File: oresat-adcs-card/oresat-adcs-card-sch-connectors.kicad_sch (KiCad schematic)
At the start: 14 parts, among them J1 J-SAMTEC-TFM-120-X1-XXX-D-RA, J3 Mezzanine Plug, J4 Mezzanine Plug, J5 Mezzanine Plug, J6 Mezzanine Plug, J7 Magnetorquer Pins

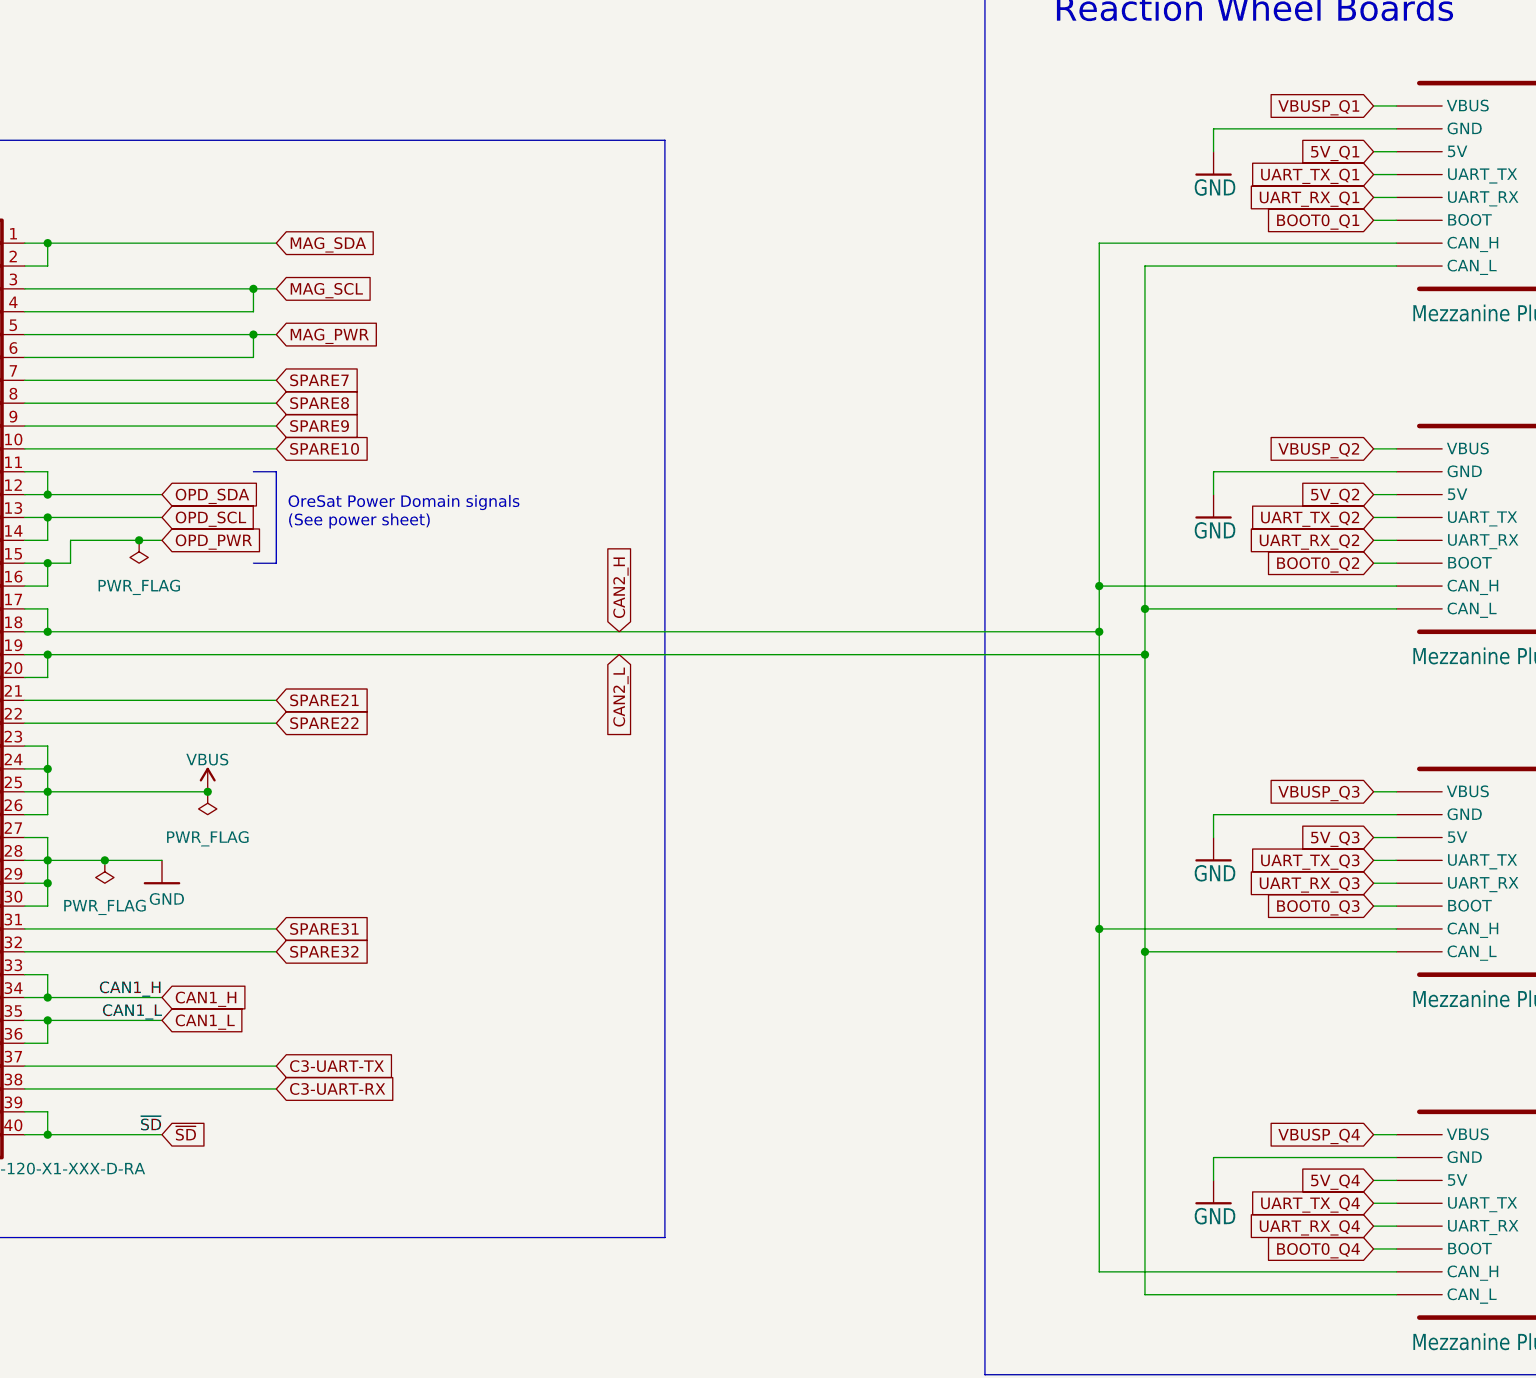
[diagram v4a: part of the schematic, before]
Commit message: Design review changes
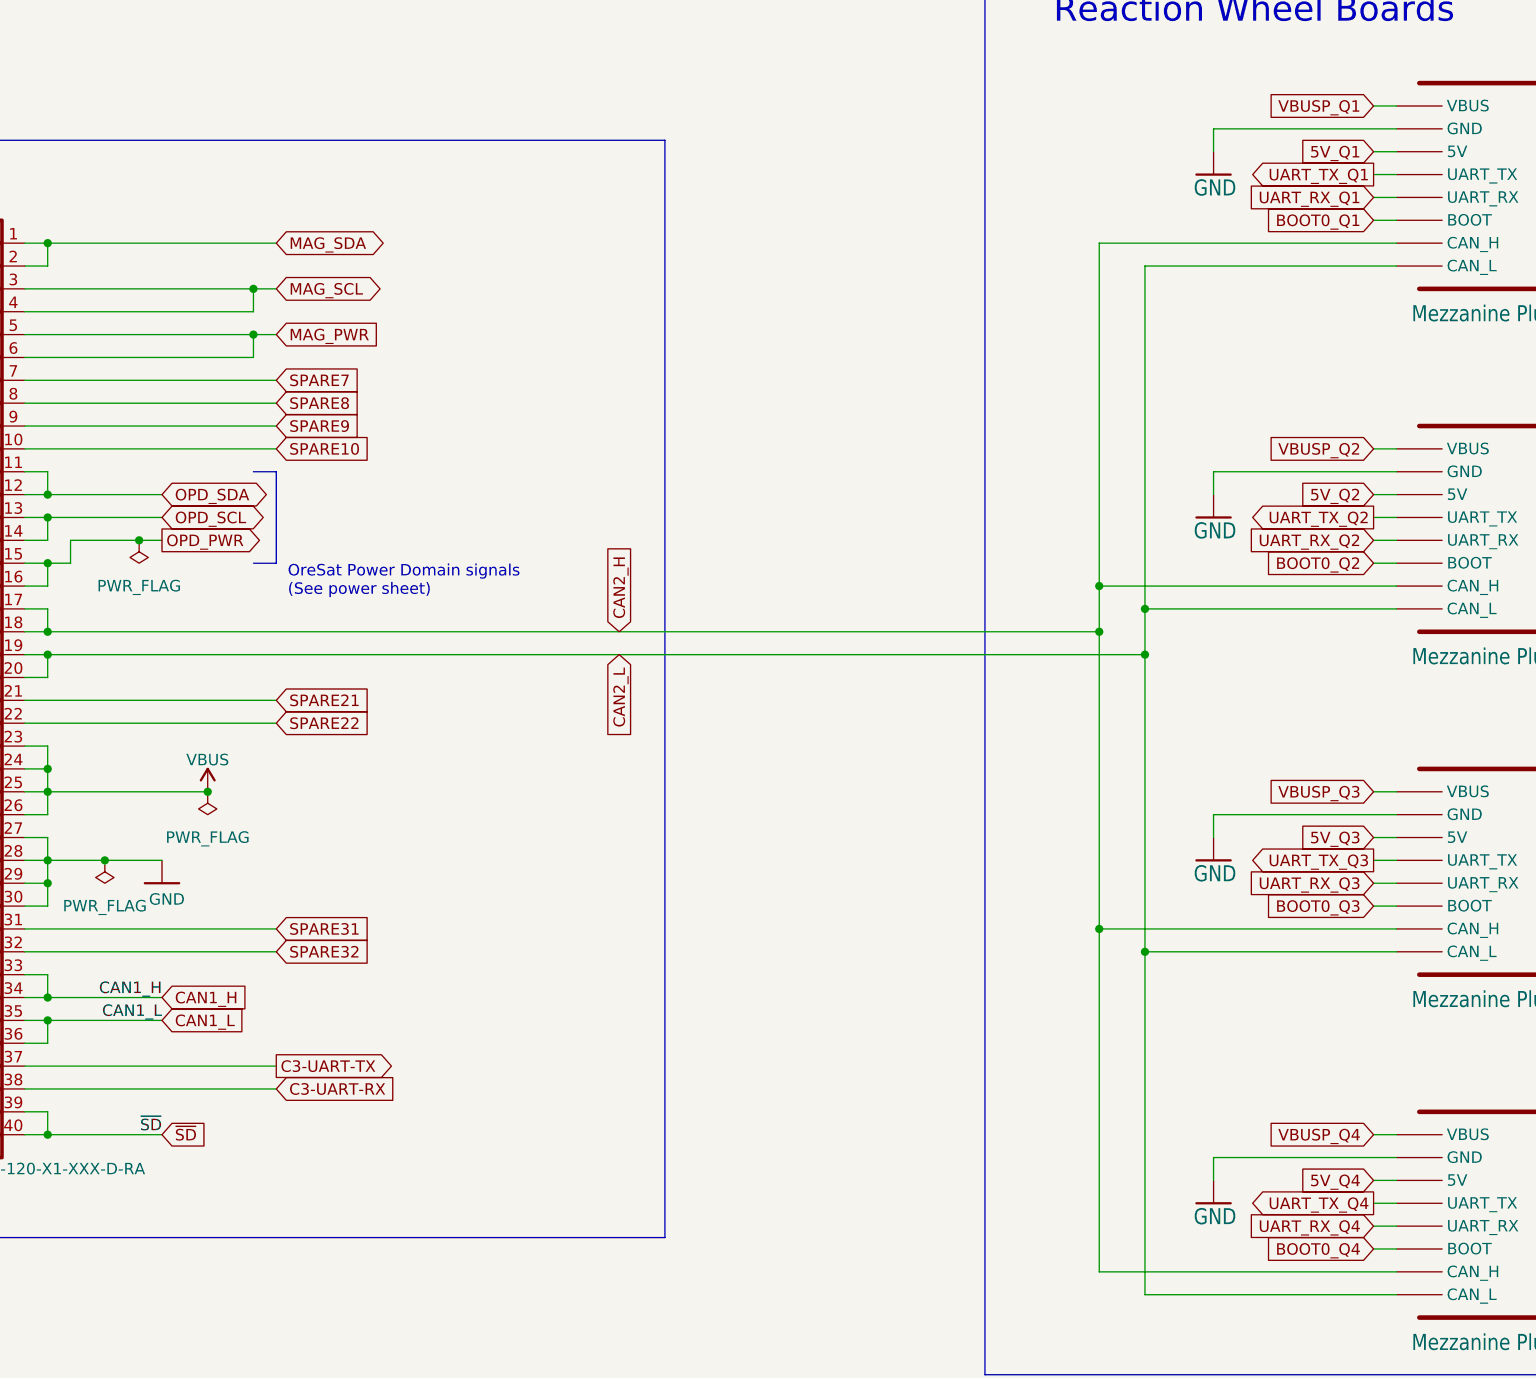
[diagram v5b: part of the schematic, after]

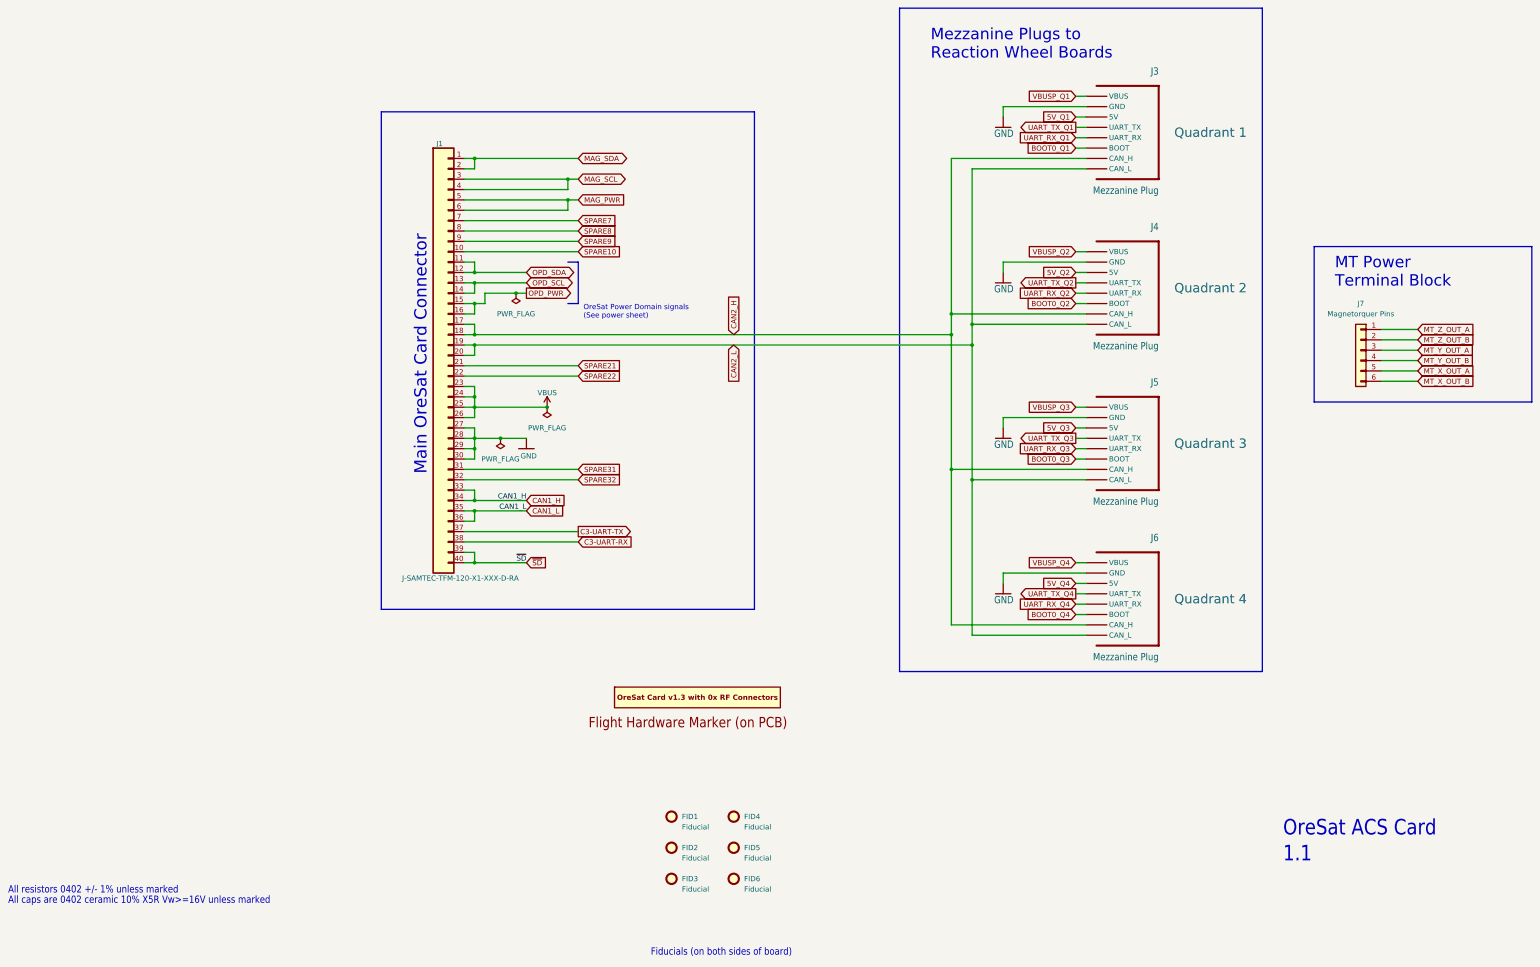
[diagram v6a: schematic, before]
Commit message: Added worksheet variables, Made OPD resistors NP appropriately, revamped the BOM table, and started working on fixing the BOM table and all the values that we seem to have lost?!
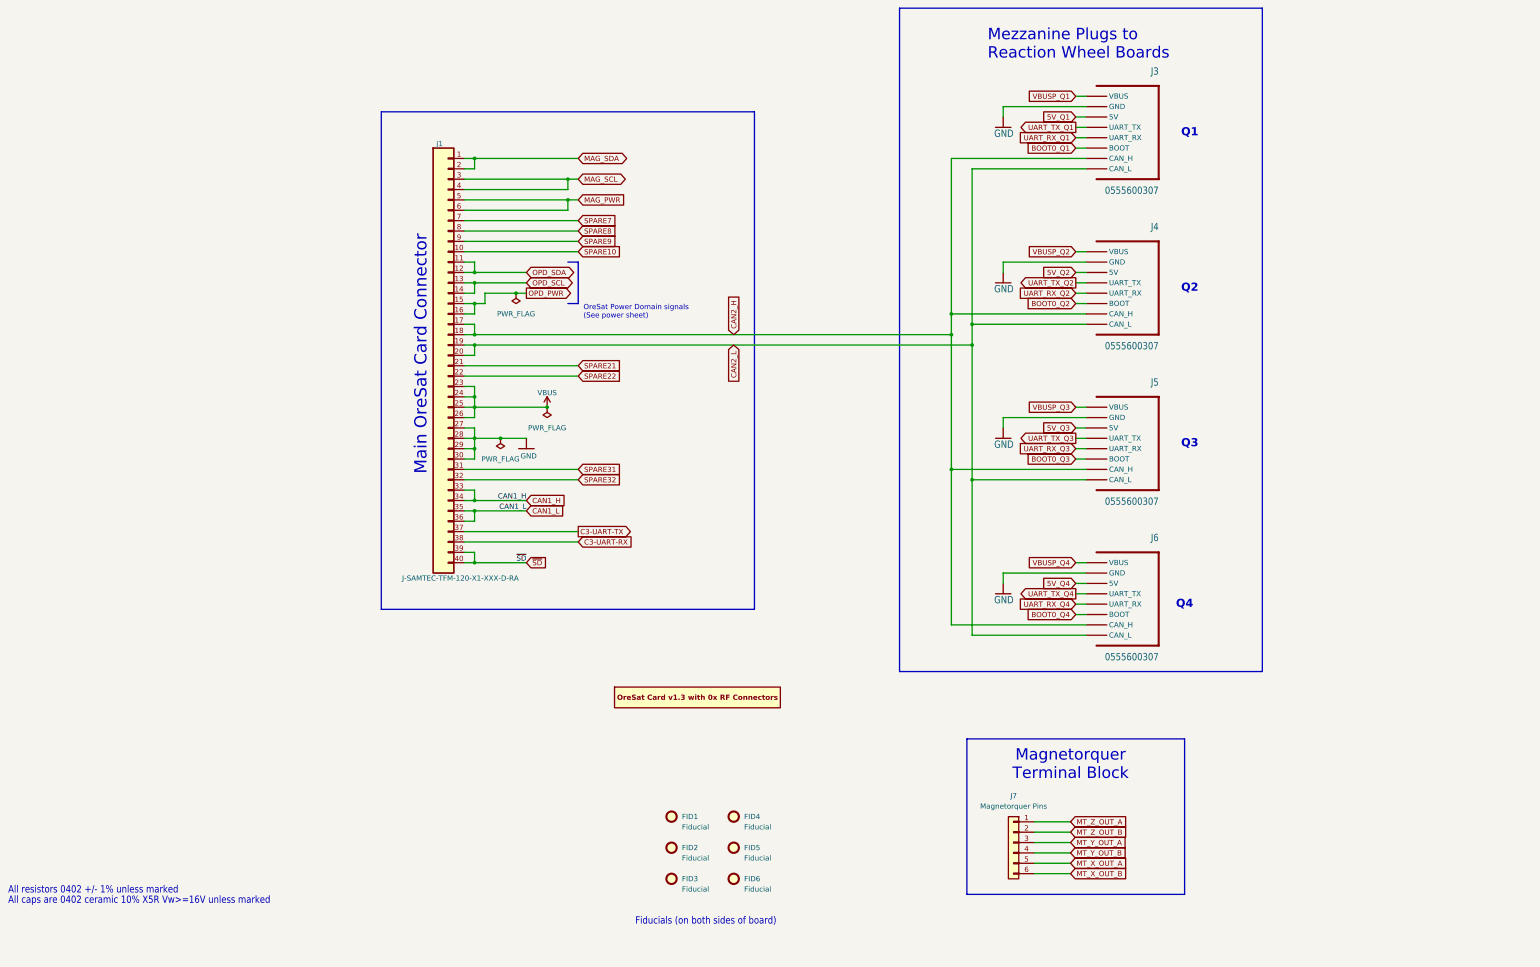
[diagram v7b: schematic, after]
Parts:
- removed U$1: FLIGHMARKERNEW, oresat-acs-card:FLIGHTMARKER_NEW_BOARDS, symbol oresat-acs-card-eagle-import:FLIGHMARKERNEW
- J3: value Mezzanine Plug -> 0555600307; DIST (none) -> Digi-Key; DPN (none) -> WM9218CT-ND; Field4 Quadrant 1 -> (none); MFR (none) -> Molex; MPN (none) -> 0555600307
- J4: value Mezzanine Plug -> 0555600307; DIST (none) -> Digi-Key; DPN (none) -> WM9218CT-ND; Field4 Quadrant 2 -> (none); MFR (none) -> Molex; MPN (none) -> 0555600307
- J5: value Mezzanine Plug -> 0555600307; DIST (none) -> Digi-Key; DPN (none) -> WM9218CT-ND; Field4 Quadrant 3 -> (none); MFR (none) -> Molex; MPN (none) -> 0555600307
- J6: value Mezzanine Plug -> 0555600307; DIST (none) -> Digi-Key; DPN (none) -> WM9218CT-ND; Field4 Quadrant 4 -> (none); MFR (none) -> Molex; MPN (none) -> 0555600307
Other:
- note added: "Magnetorquer Terminal Block"
- note added: "Q1"
- note added: "Q2"
- note added: "Q3"
- note added: "Q4"
- note removed: "1.1"
- note removed: "MT Power Terminal Block"
- note removed: "OreSat ACS Card"
- title: (none) -> OreSat ADCS Card
- moved on the sheet: J7
